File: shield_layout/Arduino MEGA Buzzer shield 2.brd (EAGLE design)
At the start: 101.6 x 64.8 mm, 36 parts

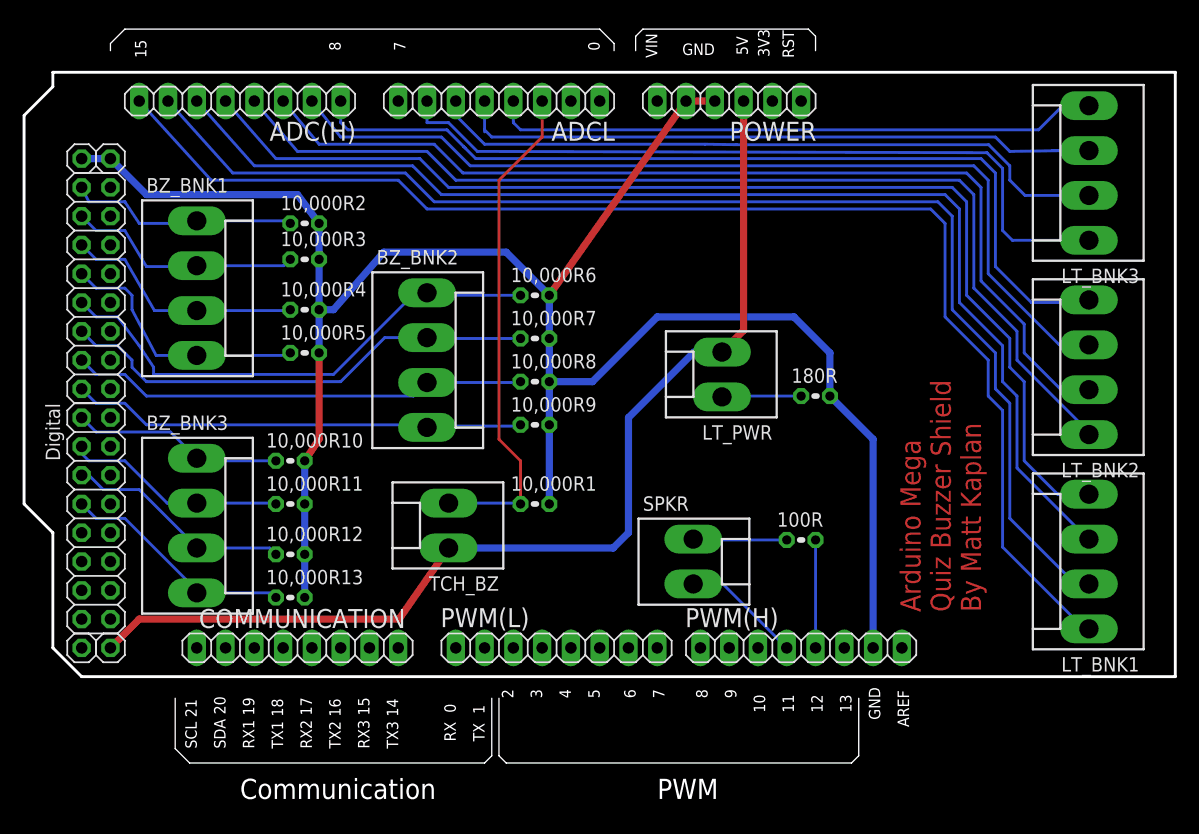
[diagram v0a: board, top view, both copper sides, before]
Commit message: update buzzer shield board layout to resize molex connectors and resistors
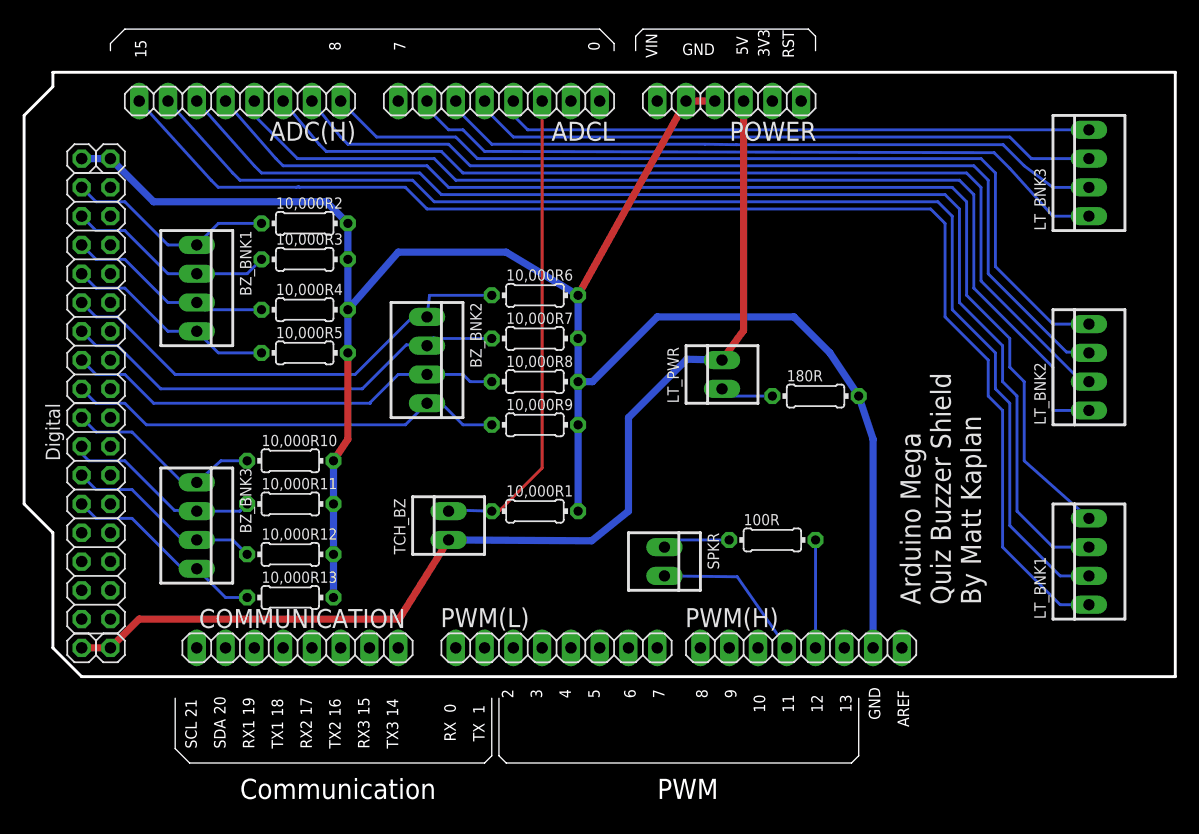
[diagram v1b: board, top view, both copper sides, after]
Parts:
- 10,000R1, 10,000R10, 10,000R11, 10,000R12, 10,000R13, 10,000R2, 10,000R3, 10,000R4, 10,000R5, 10,000R6, 10,000R7, 10,000R8, 10,000R9, 100R, 180R: device resistor:0204V -> eagle-ltspice:0204/7
- BZ_BNK1, BZ_BNK2, BZ_BNK3, LT_BNK1, LT_BNK2, LT_BNK3: device con-molex:KK-156-4 -> con-molex:22-23-2041
- LT_PWR, SPKR, TCH_BZ: device con-molex:KK-156-2 -> con-molex:22-23-2021
- moved SPKR 2.54 mm to (6.99, 43.2)
- moved 100R 2.54 mm to (16.5, 45.1)
- moved 10,000R1 0.63 mm to (-4.45, 47.6)
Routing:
- net ADC6: track 67.9 -> 63.1 mm
- net DIG47: track 23.0 -> 18.8 mm
- net PWM11: track 11.9 -> 15.3 mm
- net DIG49: track 21.6 -> 18.2 mm
- net DIG31: track 20.7 -> 18.0 mm
- net DIG45: track 45.3 -> 42.6 mm
- net ADC13: track 105.4 -> 107.9 mm
- net DIG51: track 21.0 -> 18.5 mm
- net ADC4: track 58.2 -> 55.8 mm
- net DIG43: track 42.6 -> 40.3 mm
- net ADC2: track 44.3 -> 42.2 mm
- net GND: track 179.1 -> 177.1 mm
- net DIG35: track 19.6 -> 17.6 mm
- net SPKR$1: track 8.44 -> 6.43 mm
- net N$2: track 7.02 -> 5.01 mm
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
